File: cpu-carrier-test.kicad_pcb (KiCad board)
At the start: 4 copper layers, 100 x 85 mm, 93 parts, among them J1 Micro_SD_Card_Det, J1101 USB_miniB, J1102 USB_C_Receptacle_USB2.0, J19 SFP, J20 SFP_CAGE, J4 JTAG, J5 Molex_0936263508, J6 USB_A, SW1 SW_Push, U1 TXS0108EPW, U1101 USB3740B-AI9, U1102 UTC2000, U1103 FT232RL, U1104 74LVC1G00, U1105 SC185, U6 PCA9546AD, U8 74AC125, U9 TPS2051B

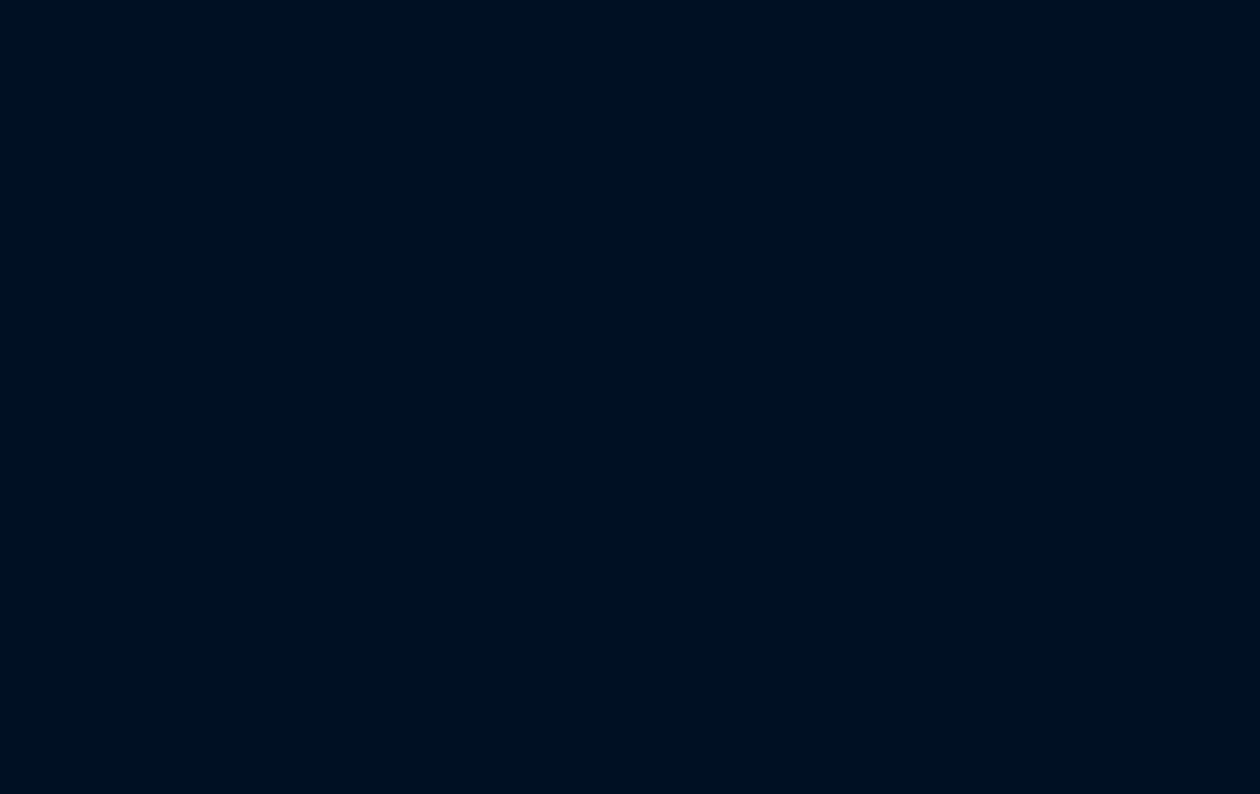
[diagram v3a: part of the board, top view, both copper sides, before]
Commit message: merged lan9254 module
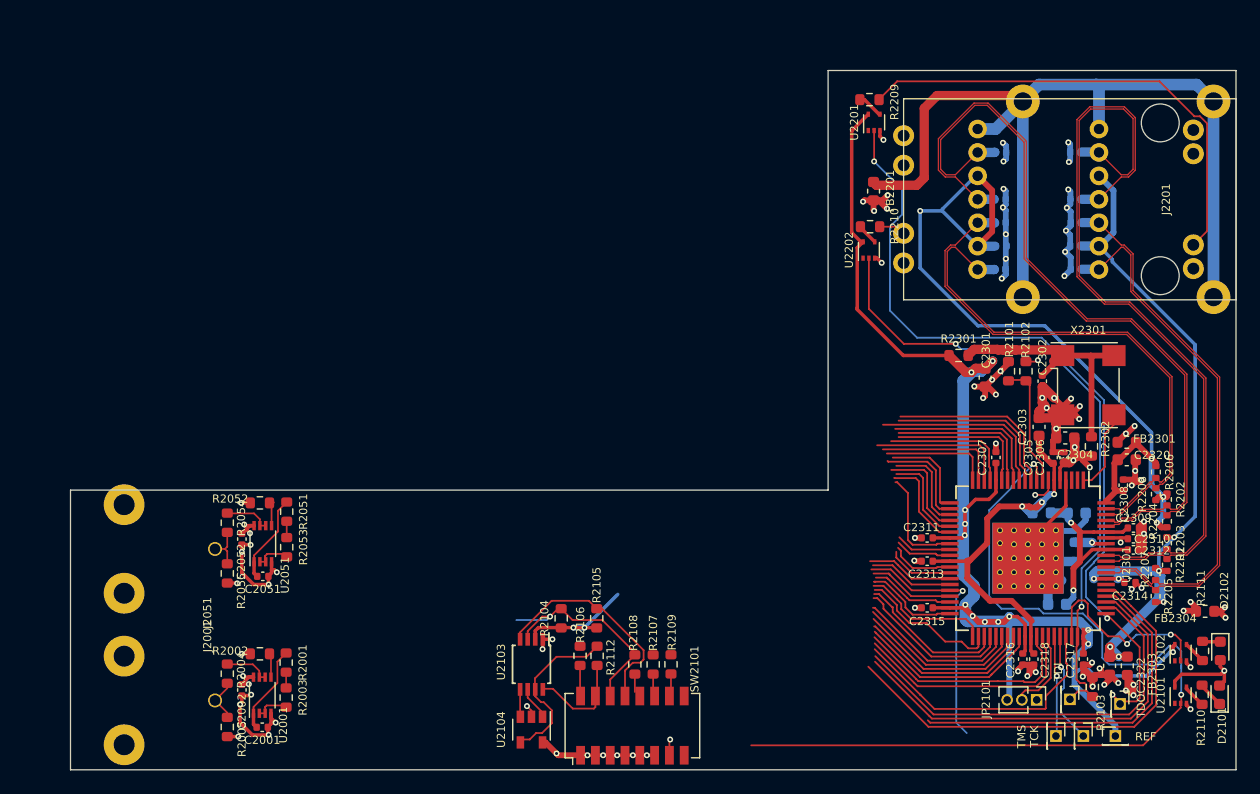
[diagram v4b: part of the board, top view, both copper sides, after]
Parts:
- added C2001: 100n, Capacitor_SMD:C_0402_1005Metric, F.Cu at (168.0, 198.7)
- added C2002: 100n, Capacitor_SMD:C_0402_1005Metric, F.Cu at (166.2, 195.5)
- added C2051: 100n, Capacitor_SMD:C_0402_1005Metric, F.Cu at (168.1, 185.8)
- added C2052: 100n, Capacitor_SMD:C_0402_1005Metric, F.Cu at (166.2, 182.6)
- added C2201: 10p, Capacitor_SMD:C_0402_1005Metric, B.Cu at (237.8, 149.3)
- added C2202: 10p, Capacitor_SMD:C_0402_1005Metric, B.Cu at (231.3, 149.4)
- added C2203: 10p, Capacitor_SMD:C_0402_1005Metric, B.Cu at (237.8, 153.4)
- added C2204: 10p, Capacitor_SMD:C_0402_1005Metric, B.Cu at (231.3, 153.4)
- added C2205: 10p, Capacitor_SMD:C_0402_1005Metric, B.Cu at (237.8, 155.4)
- added C2206: 10p, Capacitor_SMD:C_0402_1005Metric, B.Cu at (231.3, 155.4)
- added C2207: 10p, Capacitor_SMD:C_0402_1005Metric, B.Cu at (237.8, 159.4)
- added C2208: 10p, Capacitor_SMD:C_0402_1005Metric, B.Cu at (231.3, 159.4)
- added C2209: 10p, Capacitor_SMD:C_0402_1005Metric, B.Cu at (237.8, 157.4)
- added C2210: 10p, Capacitor_SMD:C_0402_1005Metric, B.Cu at (231.4, 157.4)
- added C2301: 1u_loESR, Capacitor_SMD:C_0603_1608Metric, F.Cu at (230.0, 168.7)
- added C2302: 100n, Capacitor_SMD:C_0402_1005Metric, F.Cu at (234.9, 169.0)
- added C2303: 1u_loESR, Capacitor_SMD:C_0603_1608Metric, F.Cu at (234.7, 172.9)
- added C2304: 1u_loESR, Capacitor_SMD:C_0603_1608Metric, F.Cu at (236.9, 173.9)
- added C2305: 470p, Capacitor_SMD:C_0402_1005Metric, F.Cu at (235.8, 175.6)
- added C2306: 100n, Capacitor_SMD:C_0402_1005Metric, F.Cu at (236.8, 175.6)
- added C2307: 100n, Capacitor_SMD:C_0402_1005Metric, F.Cu at (230.9, 175.6)
- added C2308: 100n, Capacitor_SMD:C_0402_1005Metric, F.Cu at (241.9, 177.9)
- added C2309: 100n, Capacitor_SMD:C_0402_1005Metric, F.Cu at (242.8, 181.6)
- added C2310: 100n, Capacitor_SMD:C_0402_1005Metric, F.Cu at (242.8, 182.5)
- added C2311: 100n, Capacitor_SMD:C_0402_1005Metric, F.Cu at (225.1, 182.4)
- added C2312: 100n, Capacitor_SMD:C_0402_1005Metric, F.Cu at (242.8, 183.5)
- added C2313: 100n, Capacitor_SMD:C_0402_1005Metric, F.Cu at (225.1, 184.4)
- added C2314: 100n, Capacitor_SMD:C_0402_1005Metric, F.Cu at (242.4, 186.3)
- added C2315: 100n, Capacitor_SMD:C_0402_1005Metric, F.Cu at (225.1, 188.4)
- added C2316: 100n, Capacitor_SMD:C_0402_1005Metric, F.Cu at (233.2, 192.8)
- added C2317: 100n, Capacitor_SMD:C_0402_1005Metric, F.Cu at (238.4, 192.8)
- added C2318: 100n, Capacitor_SMD:C_0402_1005Metric, F.Cu at (234.2, 192.8)
- added C2319: 1u, Capacitor_SMD:C_0603_1608Metric, B.Cu at (237.9, 180.3)
- added C2320: 1u, Capacitor_SMD:C_0603_1608Metric, F.Cu at (242.2, 175.8)
- added C2321: 1u, Capacitor_SMD:C_0603_1608Metric, B.Cu at (236.2, 188.2)
- added C2322: 1u, Capacitor_SMD:C_0603_1608Metric, F.Cu at (240.7, 193.4)
- added D2101: LED_Small, LED_SMD:LED_0603_1608Metric, F.Cu at (250.1, 195.9)
- added D2102: LED_Small, LED_SMD:LED_0603_1608Metric, F.Cu at (250.2, 192.2)
- added FB2201: FB_250, Inductor_SMD:L_0603_1608Metric, F.Cu at (220.4, 152.7)
- added FB2301: FB_250, Inductor_SMD:L_0603_1608Metric, F.Cu at (242.2, 174.2)
- added FB2302: FB_250, Inductor_SMD:L_0603_1608Metric, B.Cu at (234.9, 180.3)
- added FB2303: FB_250, Inductor_SMD:L_0603_1608Metric, F.Cu at (242.2, 193.4)
- added FB2304: FB_250, Inductor_SMD:L_0603_1608Metric, F.Cu at (248.9, 188.8)
- added J2001: BNC, proj_footprints:BNC_Molex_0731713150, F.Cu at (156.2, 196.4)
- added J2051: BNC, proj_footprints:BNC_Molex_0731713150, F.Cu at (156.2, 183.4)
- added J2201: BEL_0845_2G1T_H5, proj_footprints:BEL_0845-2G1T-H5, F.Cu at (245.1, 153.4)
- added JP2101: Jumper_3_Bridged12, Connector_PinHeader_1.27mm:PinHeader_1x03_P1.27mm_Vertical, F.Cu at (234.4, 196.3)
- added R2001: 100k, Resistor_SMD:R_0603_1608Metric, F.Cu at (170.1, 193.2)
- added R2002: 2k2, Resistor_SMD:R_0603_1608Metric, F.Cu at (167.8, 192.4)
- added R2003: 100, Resistor_SMD:R_0603_1608Metric, F.Cu at (170.1, 196.2)
- added R2004: 0, Resistor_SMD:R_0603_1608Metric, F.Cu at (165.0, 194.1)
- added R2005: 100k, Resistor_SMD:R_0603_1608Metric, F.Cu at (165.0, 198.7)
- added R2051: 100k, Resistor_SMD:R_0603_1608Metric, F.Cu at (170.1, 180.2)
- added R2052: 2k2, Resistor_SMD:R_0603_1608Metric, F.Cu at (167.8, 179.4)
- added R2053: 100, Resistor_SMD:R_0603_1608Metric, F.Cu at (170.1, 183.2)
- added R2054: 0, Resistor_SMD:R_0603_1608Metric, F.Cu at (165.0, 181.2)
- added R2055: 100k, Resistor_SMD:R_0603_1608Metric, F.Cu at (165.0, 185.5)
- added R2101: 1k, Resistor_SMD:R_0603_1608Metric, F.Cu at (232.0, 168.2)
- added R2102: 1k, Resistor_SMD:R_0603_1608Metric, F.Cu at (233.5, 168.2)
- added R2103: 1k, Resistor_SMD:R_0603_1608Metric, F.Cu at (239.2, 195.2)
- added R2104: 10k, Resistor_SMD:R_0603_1608Metric, F.Cu at (193.7, 189.3)
- added R2105: 10k, Resistor_SMD:R_0603_1608Metric, F.Cu at (196.7, 189.3)
- added R2106: 1k, Resistor_SMD:R_0603_1608Metric, F.Cu at (195.3, 192.6)
- added R2107: 1k, Resistor_SMD:R_0603_1608Metric, F.Cu at (201.5, 193.3)
- added R2108: 1k, Resistor_SMD:R_0603_1608Metric, F.Cu at (200.0, 193.3)
- added R2109: 4k7, Resistor_SMD:R_0603_1608Metric, F.Cu at (203.1, 193.3)
- added R2110: 100, Resistor_SMD:R_0603_1608Metric, F.Cu at (248.6, 195.9)
- added R2111: 100, Resistor_SMD:R_0603_1608Metric, F.Cu at (248.7, 192.2)
- added R2112: 10k, Resistor_SMD:R_0603_1608Metric, F.Cu at (196.7, 192.6)
- added R2201: 50, Resistor_SMD:R_0402_1005Metric, F.Cu at (245.6, 184.8)
- added R2202: 50, Resistor_SMD:R_0402_1005Metric, F.Cu at (245.6, 179.2)
- added R2203: 50, Resistor_SMD:R_0402_1005Metric, F.Cu at (245.6, 182.9)
- added R2204: 50, Resistor_SMD:R_0402_1005Metric, F.Cu at (245.6, 181.0)
- added R2205: 50, Resistor_SMD:R_0402_1005Metric, F.Cu at (244.7, 187.4)
- added R2206: 50, Resistor_SMD:R_0402_1005Metric, F.Cu at (244.7, 176.8)
- added R2207: 50, Resistor_SMD:R_0402_1005Metric, F.Cu at (244.7, 185.6)
- added R2208: 50, Resistor_SMD:R_0402_1005Metric, F.Cu at (244.7, 178.7)
- added R2209: 100, Resistor_SMD:R_0603_1608Metric, F.Cu at (220.1, 144.8)
- added R2210: 100, Resistor_SMD:R_0603_1608Metric, F.Cu at (220.2, 155.8)
- added R2301: 0, Resistor_SMD:R_0603_1608Metric, F.Cu at (227.8, 166.8)
- added R2302: 0, Resistor_SMD:R_0603_1608Metric, F.Cu at (239.2, 174.6)
- added R2303: 12.1k, Resistor_SMD:R_0603_1608Metric, B.Cu at (237.8, 183.7)
- added SW2101: SW_DIP_x08, Button_Switch_SMD:SW_DIP_SPSTx08_Slide_Copal_CHS-08A_W5.08mm_P1.27mm_JPin, F.Cu at (199.8, 198.6)
- added TP2301: TDO, Connector_PinHeader_1.27mm:PinHeader_1x01_P1.27mm_Vertical, F.Cu at (241.6, 196.7)
- added TP2302: TDI, Connector_PinHeader_1.27mm:PinHeader_1x01_P1.27mm_Vertical, F.Cu at (237.3, 196.3)
- added TP2303: TCK, Connector_PinHeader_1.27mm:PinHeader_1x01_P1.27mm_Vertical, F.Cu at (238.4, 199.4)
- added TP2304: TMS, Connector_PinHeader_1.27mm:PinHeader_1x01_P1.27mm_Vertical, F.Cu at (236.1, 199.4)
- added TP2305: REF, Connector_PinHeader_1.27mm:PinHeader_1x01_P1.27mm_Vertical, F.Cu at (241.2, 199.4)
- added U2001: 74LVC2T45DC, Package_SO:VSSOP-8_2.3x2mm_P0.5mm, F.Cu at (168.0, 195.9)
- added U2051: 74LVC2T45DC, Package_SO:VSSOP-8_2.3x2mm_P0.5mm, F.Cu at (168.1, 182.9)
- added U2101: 74LVC1G06, Package_TO_SOT_SMD:SOT-553, F.Cu at (246.8, 195.9)
- added U2102: 74LVC1G06, Package_TO_SOT_SMD:SOT-553, F.Cu at (246.8, 192.3)
- added U2103: PCA9306, Package_SO:TSSOP-8_3x3mm_P0.65mm, F.Cu at (191.1, 193.3)
- added U2104: 24AA0x, Package_TO_SOT_SMD:SOT-23-5, F.Cu at (191.1, 198.9)
- added U2201: 74LVC1G06, Package_TO_SOT_SMD:SOT-553, F.Cu at (220.5, 146.8)
- added U2202: 74LVC1G06, Package_TO_SOT_SMD:SOT-553, F.Cu at (220.1, 157.8)
- added U2301: lan9254, proj_footprints:TQFP-80_12x12mm_P0.5mm_EP6x6mm, F.Cu at (233.7, 184.2)
- added X2301: FNETHE025, Oscillator:Oscillator_SMD_Diodes_FN-4Pin_7.0x5.0mm, F.Cu at (238.9, 169.3)
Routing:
- net +1V8_lan9254: track 0.00 -> 149.9 mm, vias 0 -> 15
- net GND_lan9254: track 0.00 -> 126.7 mm, vias 0 -> 75
- net Net-(FB2201-Pad1): track 0.00 -> 80.1 mm
- net /lan9254/ERRLED: track 0.00 -> 78.8 mm, vias 0 -> 2
- net /lan9254/LINKACT0: track 0.00 -> 70.7 mm, vias 0 -> 3
- net /lan9254/VDD33TXRX2: track 0.00 -> 70.3 mm, vias 0 -> 4
- net /lan9254/VDD33TXRX1: track 0.00 -> 68.2 mm, vias 0 -> 7
- net /lan9254/rj45_ports/P0_RXD_P: track 0.00 -> 66.9 mm
- net /lan9254/rj45_ports/P0_RXD_N: track 0.00 -> 66.3 mm
- net /lan9254/rj45_ports/P1_RXD_P: track 0.00 -> 65.7 mm
- net /lan9254/rj45_ports/P1_RXD_N: track 0.00 -> 64.5 mm
- net /lan9254/LINKACT1: track 0.00 -> 56.1 mm, vias 0 -> 2
- net /lan9254/rj45_ports/P0_TXD_N: track 0.00 -> 46.6 mm
- net /lan9254/EESCL: track 0.00 -> 46.5 mm, vias 0 -> 4
- net /lan9254/rj45_ports/P1_TXD_N: track 0.00 -> 46.2 mm
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- added copper zone on In2.Cu, net +3V3_lan9254
- added copper zone on In1.Cu, net GND_lan9254
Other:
- board size 100 x 85 mm -> 151.6 x 172.3 mm
- net class diffp_ec added: clearance 0.0889, trace_width 0.0889, via_dia 0.4, via_drill 0.2

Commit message: connected lan9254 power to board power
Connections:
- C2001 pad 1: +1V8_lan9254 -> +1V8
- C2001 pad 2: GND_lan9254 -> OTG_ID
- C2002 pad 1: +3V3_lan9254 -> +3V3
- C2002 pad 2: GND_lan9254 -> OTG_ID
- C2051 pad 1: +1V8_lan9254 -> +1V8
- C2051 pad 2: GND_lan9254 -> OTG_ID
- C2052 pad 1: +3V3_lan9254 -> +3V3
- C2052 pad 2: GND_lan9254 -> OTG_ID
- C2201 pad 2: GND_lan9254 -> OTG_ID
- C2202 pad 2: GND_lan9254 -> OTG_ID
- C2203 pad 2: GND_lan9254 -> OTG_ID
- C2204 pad 2: GND_lan9254 -> OTG_ID
- C2205 pad 2: GND_lan9254 -> OTG_ID
- C2206 pad 2: GND_lan9254 -> OTG_ID
- C2207 pad 2: GND_lan9254 -> OTG_ID
- C2208 pad 2: GND_lan9254 -> OTG_ID
- C2209 pad 2: GND_lan9254 -> OTG_ID
- C2210 pad 2: GND_lan9254 -> OTG_ID
- C2301 pad 1: +1V8_lan9254 -> +1V8
- C2301 pad 2: GND_lan9254 -> OTG_ID
- C2302 pad 2: GND_lan9254 -> OTG_ID
- C2303 pad 2: GND_lan9254 -> OTG_ID
- C2304 pad 1: +3V3_lan9254 -> +3V3
- C2304 pad 2: GND_lan9254 -> OTG_ID
- C2305 pad 2: GND_lan9254 -> OTG_ID
- C2306 pad 1: +3V3_lan9254 -> +3V3
- C2306 pad 2: GND_lan9254 -> OTG_ID
- C2307 pad 1: +1V8_lan9254 -> +1V8
- C2307 pad 2: GND_lan9254 -> OTG_ID
- C2308 pad 1: GND_lan9254 -> OTG_ID
- C2309 pad 1: GND_lan9254 -> OTG_ID
- C2310 pad 1: GND_lan9254 -> OTG_ID
- C2311 pad 1: +1V8_lan9254 -> +1V8
- C2311 pad 2: GND_lan9254 -> OTG_ID
- C2312 pad 1: GND_lan9254 -> OTG_ID
- C2313 pad 2: GND_lan9254 -> OTG_ID
- C2314 pad 1: GND_lan9254 -> OTG_ID
- C2315 pad 1: +1V8_lan9254 -> +1V8
- C2315 pad 2: GND_lan9254 -> OTG_ID
- C2316 pad 1: +1V8_lan9254 -> +1V8
- C2316 pad 2: GND_lan9254 -> OTG_ID
- C2317 pad 1: +1V8_lan9254 -> +1V8
- C2317 pad 2: GND_lan9254 -> OTG_ID
- C2318 pad 2: GND_lan9254 -> OTG_ID
- C2319 pad 2: GND_lan9254 -> OTG_ID
- C2320 pad 2: GND_lan9254 -> OTG_ID
- C2321 pad 2: GND_lan9254 -> OTG_ID
- C2322 pad 2: GND_lan9254 -> OTG_ID
- D2101 pad 2: +3V3_lan9254 -> +3V3
- D2102 pad 2: +3V3_lan9254 -> +3V3
- FB2201 pad 2: GND_lan9254 -> OTG_ID
- FB2301 pad 1: +3V3_lan9254 -> +3V3
- FB2303 pad 1: +3V3_lan9254 -> +3V3
- FB2304 pad 1: +3V3_lan9254 -> +3V3
- J2001 pad 2: GND_lan9254 -> OTG_ID
- J2051 pad 2: GND_lan9254 -> OTG_ID
- J2201 pad 15: +3V3_lan9254 -> +3V3
- J2201 pad 19: +3V3_lan9254 -> +3V3
- JP2101 pad 1: GND_lan9254 -> OTG_ID
- JP2101 pad 3: +1V8_lan9254 -> +1V8
- R2001 pad 1: +1V8_lan9254 -> +1V8
- R2002 pad 2: GND_lan9254 -> OTG_ID
- R2005 pad 2: GND_lan9254 -> OTG_ID
- R2051 pad 1: +1V8_lan9254 -> +1V8
- R2052 pad 2: GND_lan9254 -> OTG_ID
- R2055 pad 2: GND_lan9254 -> OTG_ID
- R2101 pad 2: GND_lan9254 -> OTG_ID
- R2102 pad 2: +3V3_lan9254 -> +3V3
- R2103 pad 2: GND_lan9254 -> OTG_ID
- R2104 pad 1: +1V8_lan9254 -> +1V8
- R2105 pad 1: +1V8_lan9254 -> +1V8
- R2301 pad 1: +1V8_lan9254 -> +1V8
- R2302 pad 1: +3V3_lan9254 -> +3V3
- R2303 pad 1: GND_lan9254 -> OTG_ID
- SW2101 pad 1: GND_lan9254 -> OTG_ID
- SW2101 pad 2: GND_lan9254 -> OTG_ID
- SW2101 pad 3: GND_lan9254 -> OTG_ID
- SW2101 pad 4: GND_lan9254 -> OTG_ID
- SW2101 pad 5: GND_lan9254 -> OTG_ID
- SW2101 pad 6: GND_lan9254 -> OTG_ID
- SW2101 pad 7: +3V3_lan9254 -> +3V3
- TP2305 pad 1: +1V8_lan9254 -> +1V8
- U2001 pad 1: +1V8_lan9254 -> +1V8
- U2001 pad 4: GND_lan9254 -> OTG_ID
- U2001 pad 8: +3V3_lan9254 -> +3V3
- U2051 pad 1: +1V8_lan9254 -> +1V8
- U2051 pad 4: GND_lan9254 -> OTG_ID
- U2051 pad 8: +3V3_lan9254 -> +3V3
- U2101 pad 3: GND_lan9254 -> OTG_ID
- U2101 pad 5: +3V3_lan9254 -> +3V3
- U2102 pad 3: GND_lan9254 -> OTG_ID
- U2102 pad 5: +1V8_lan9254 -> +1V8
- U2103 pad 1: GND_lan9254 -> OTG_ID
- U2103 pad 2: +1V8_lan9254 -> +1V8
- U2104 pad 2: GND_lan9254 -> OTG_ID
- U2104 pad 5: GND_lan9254 -> OTG_ID
- U2201 pad 3: GND_lan9254 -> OTG_ID
- U2201 pad 5: +1V8_lan9254 -> +1V8
- U2202 pad 3: GND_lan9254 -> OTG_ID
- U2202 pad 5: +1V8_lan9254 -> +1V8
- U2301 pad 16: +1V8_lan9254 -> +1V8
- U2301 pad 27: +1V8_lan9254 -> +1V8
- U2301 pad 39: +1V8_lan9254 -> +1V8
- U2301 pad 4: GND_lan9254 -> OTG_ID
- U2301 pad 5: +3V3_lan9254 -> +3V3
- U2301 pad 50: +1V8_lan9254 -> +1V8
- U2301 pad 60: +1V8_lan9254 -> +1V8
- U2301 pad 7: +3V3_lan9254 -> +3V3
- U2301 pad 81: GND_lan9254 -> OTG_ID
- X2301 pad 2: GND_lan9254 -> OTG_ID
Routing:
- net +1V8: track 71.4 -> 221.3 mm, vias 3 -> 18
- net +1V8_lan9254: track 149.9 -> 0.00 mm, vias 15 -> 0
- net GND_lan9254: track 126.7 -> 0.00 mm, vias 75 -> 0
- net OTG_ID: track 263.5 -> 390.1 mm, vias 145 -> 220
- net +3V3: track 258.5 -> 292.0 mm, vias 11 -> 29
- net +3V3_lan9254: track 33.5 -> 0.00 mm, vias 18 -> 0
- removed copper zone on In2.Cu, net +3V3_lan9254
- removed copper zone on In1.Cu, net GND_lan9254

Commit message: connected lan9254 i2c to baseboard SDA0/SDC0
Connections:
- R2112 pad 1: /lan9254/I2C_VCC -> +3V3
- U2103 pad 5: /lan9254/SDA_3V3 -> SDA0
- U2103 pad 6: /lan9254/SCL_3V3 -> SCL0
- U2103 pad 7: /lan9254/I2C_VCC -> +3V3
- U2104 pad 1: /lan9254/SCL_3V3 -> SCL0
- U2104 pad 3: /lan9254/SDA_3V3 -> SDA0
- U2104 pad 4: /lan9254/I2C_VCC -> +3V3
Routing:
- net /lan9254/I2C_VCC: track 14.4 -> 0.00 mm
- net +3V3: track 292.0 -> 306.4 mm
- net SCL0: track 3.90 -> 6.81 mm
- net /lan9254/SCL_3V3: track 2.91 -> 0.00 mm
- net SDA0: track 4.05 -> 6.38 mm
- net /lan9254/SDA_3V3: track 2.33 -> 0.00 mm

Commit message: converted local- to global labels for B34/B34 B2B pins
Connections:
- net /B2B Connector/B34_L10_N renamed B34_L10_N
- net /B2B Connector/B34_L10_P renamed B34_L10_P
- net /B2B Connector/B34_L11_N renamed B34_L11_N
- net /B2B Connector/B34_L11_P renamed B34_L11_P
- net /B2B Connector/B34_L12_N renamed B34_L12_N
- net /B2B Connector/B34_L12_P renamed B34_L12_P
- net /B2B Connector/B34_L13_N renamed B34_L13_N
- net /B2B Connector/B34_L13_P renamed B34_L13_P
- net /B2B Connector/B34_L14_N renamed B34_L14_N
- net /B2B Connector/B34_L14_P renamed B34_L14_P
- net /B2B Connector/B34_L15_N renamed B34_L15_N
- net /B2B Connector/B34_L15_P renamed B34_L15_P
- net /B2B Connector/B34_L16_N renamed B34_L16_N
- net /B2B Connector/B34_L16_P renamed B34_L16_P
- net /B2B Connector/B34_L17_N renamed B34_L17_N
- net /B2B Connector/B34_L17_P renamed B34_L17_P
- net /B2B Connector/B34_L18_N renamed B34_L18_N
- net /B2B Connector/B34_L18_P renamed B34_L18_P
- net /B2B Connector/B34_L20_N renamed B34_L20_N
- net /B2B Connector/B34_L20_P renamed B34_L20_P
- net /B2B Connector/B34_L21_N renamed B34_L21_N
- net /B2B Connector/B34_L21_P renamed B34_L21_P
- net /B2B Connector/B34_L22_N renamed B34_L22_N
- net /B2B Connector/B34_L22_P renamed B34_L22_P
- net /B2B Connector/B34_L23_N renamed B34_L23_N
- net /B2B Connector/B34_L23_P renamed B34_L23_P
- net /B2B Connector/B34_L2_N renamed B34_L2_N
- net /B2B Connector/B34_L2_P renamed B34_L2_P
- net /B2B Connector/B34_L6_N renamed B34_L6_N
- net /B2B Connector/B34_L6_P renamed B34_L6_P
- net /B2B Connector/B34_L7_N renamed B34_L7_N
- net /B2B Connector/B34_L7_P renamed B34_L7_P
- net /B2B Connector/B34_L8_N renamed B34_L8_N
- net /B2B Connector/B34_L8_P renamed B34_L8_P
- net /B2B Connector/B35_L0 renamed B35_L0
- net /B2B Connector/B35_L10_N renamed B35_L10_N
- net /B2B Connector/B35_L10_P renamed B35_L10_P
- net /B2B Connector/B35_L11_N renamed B35_L11_N
- net /B2B Connector/B35_L11_P renamed B35_L11_P
- net /B2B Connector/B35_L12_N renamed B35_L12_N
- net /B2B Connector/B35_L12_P renamed B35_L12_P
- net /B2B Connector/B35_L13_N renamed B35_L13_N
- net /B2B Connector/B35_L13_P renamed B35_L13_P
- net /B2B Connector/B35_L14_N renamed B35_L14_N
- net /B2B Connector/B35_L14_P renamed B35_L14_P
- net /B2B Connector/B35_L15_N renamed B35_L15_N
- net /B2B Connector/B35_L15_P renamed B35_L15_P
- net /B2B Connector/B35_L16_N renamed B35_L16_N
- net /B2B Connector/B35_L16_P renamed B35_L16_P
- net /B2B Connector/B35_L17_N renamed B35_L17_N
- net /B2B Connector/B35_L17_P renamed B35_L17_P
- net /B2B Connector/B35_L18_N renamed B35_L18_N
- net /B2B Connector/B35_L18_P renamed B35_L18_P
- net /B2B Connector/B35_L19_N renamed B35_L19_N
- net /B2B Connector/B35_L19_P renamed B35_L19_P
- net /B2B Connector/B35_L1_N renamed B35_L1_N
- net /B2B Connector/B35_L1_P renamed B35_L1_P
- net /B2B Connector/B35_L20_N renamed B35_L20_N
- net /B2B Connector/B35_L20_P renamed B35_L20_P
- net /B2B Connector/B35_L21_N renamed B35_L21_N
- net /B2B Connector/B35_L21_P renamed B35_L21_P
- net /B2B Connector/B35_L22_N renamed B35_L22_N
- net /B2B Connector/B35_L22_P renamed B35_L22_P
- net /B2B Connector/B35_L23_N renamed B35_L23_N
- net /B2B Connector/B35_L23_P renamed B35_L23_P
- net /B2B Connector/B35_L24_N renamed B35_L24_N
- net /B2B Connector/B35_L24_P renamed B35_L24_P
- net /B2B Connector/B35_L25 renamed B35_L25
- net /B2B Connector/B35_L2_N renamed B35_L2_N
- net /B2B Connector/B35_L2_P renamed B35_L2_P
- net /B2B Connector/B35_L3_N renamed B35_L3_N
- net /B2B Connector/B35_L3_P renamed B35_L3_P
- net /B2B Connector/B35_L4_N renamed B35_L4_N
- net /B2B Connector/B35_L4_P renamed B35_L4_P
- net /B2B Connector/B35_L5_N renamed B35_L5_N
- net /B2B Connector/B35_L5_P renamed B35_L5_P
- net /B2B Connector/B35_L6_N renamed B35_L6_N
- net /B2B Connector/B35_L6_P renamed B35_L6_P
- net /B2B Connector/B35_L7_N renamed B35_L7_N
- net /B2B Connector/B35_L7_P renamed B35_L7_P
- net /B2B Connector/B35_L8_N renamed B35_L8_N
- net /B2B Connector/B35_L8_P renamed B35_L8_P
- net /B2B Connector/B35_L9_N renamed B35_L9_N
- net /B2B Connector/B35_L9_P renamed B35_L9_P
